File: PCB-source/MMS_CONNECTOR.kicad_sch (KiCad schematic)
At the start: 5 parts, among them J9 RJ45_LED_Shielded

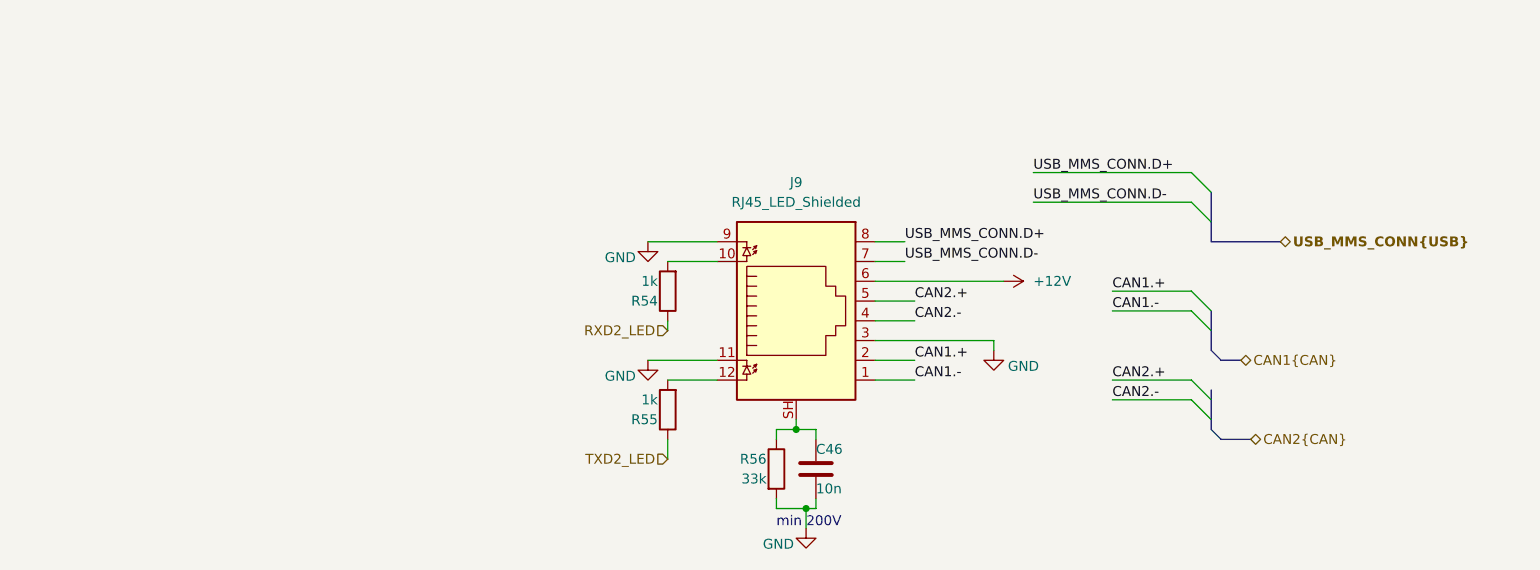
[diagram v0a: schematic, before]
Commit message: Finish component and diffpair placement
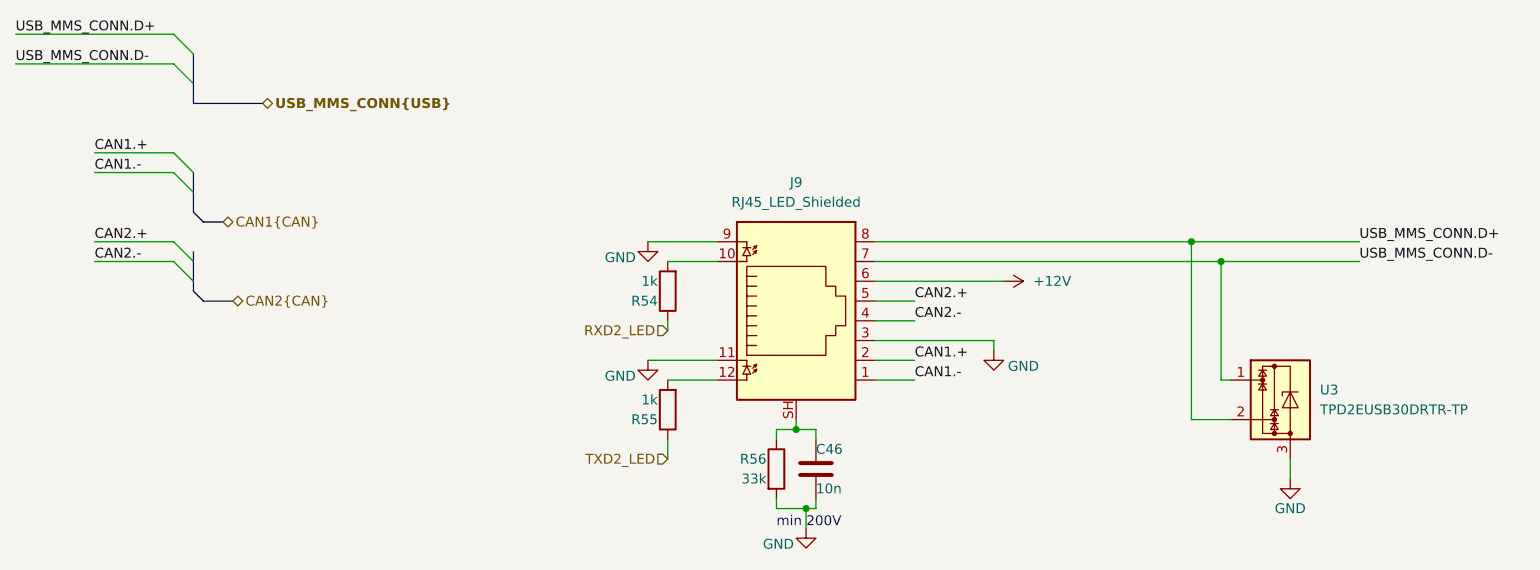
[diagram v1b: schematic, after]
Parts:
- added U3: TPD2EUSB30DRTR-TP, Package_TO_SOT_SMD:SOT-723, symbol Power_Protection:TPD2E2U06DCK
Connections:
- net GND: now also U3.3
- net USB_MMS_CONN.D+: now also U3.2
- net USB_MMS_CONN.D-: now also U3.1
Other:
- title: MMS2 -> Mini moducard connector
